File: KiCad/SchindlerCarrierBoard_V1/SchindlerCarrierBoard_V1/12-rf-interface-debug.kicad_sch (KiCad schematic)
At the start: 13 parts, among them J1200 u.FL -> A3, J1201 6-pin -> A3, J1202 JTAG, J1203 UART debug, J1204 2x20 expansion, SW1200 boot strap, SW1201 PS POR, SW1202 PL reset

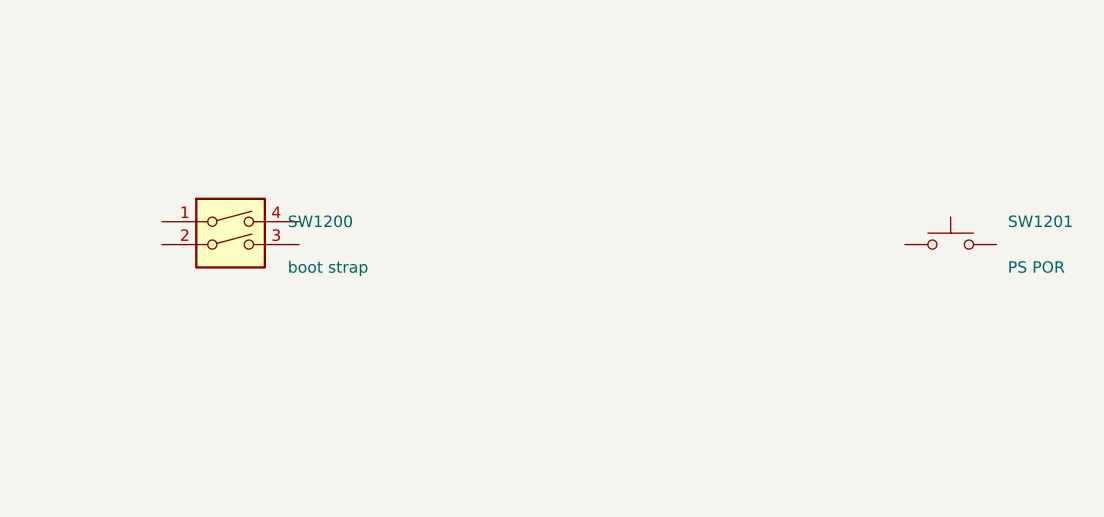
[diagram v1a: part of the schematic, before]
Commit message: Schindler carrier: ADV7511 R_EXT/AVDD fix + symbol relabel; 116 PL nets wired; connector/riser decisions
- U403 ADV7511: add R406 (887R 1%) pin28 R_EXT->GND; wire pin29 AVDD->+1V8_A (match 34/41).
  Sheet-4 ERC pin_not_connected 2->0. Fixes missing TMDS bias ref + unpowered AVDD
  (would-not-work HDMI-out bug, caught pre-fab).
- JustinLibrary ADV7511KSTZ symbol relabel: pin2 SYNC->VSYNC, 28 EXT->R_EXT, 29 R_EXT->AVDD
  (cosmetic; connectivity is by pin number). [NOTE: JustinLibrary is unversioned/external — not in this repo; see report.]
- Pin-lock: 116 PL nets wired; ERC unconnected 899->668; schindler_plio.xdc + pin-lock-assignment.md.
- Connector domain + analog I/O riser decided (connector-domain.md); riser-mezzanine-plan.md rev2
  (gated proposal, not implemented).
- bom-v1 (R406), refdes-map (R406 + symbol-mislabel note), changelog.

Deferred to next commit (kept out so this push stays honest): eeschema Update Symbols from
Library on U403 (display refresh); netlist regen; HDMI +5V power_pin_not_driven x2 (J400/J401.18)
verification; riser stays gated.

Co-Authored-By: Claude Opus 4.8 (1M context) <noreply@anthropic.com>
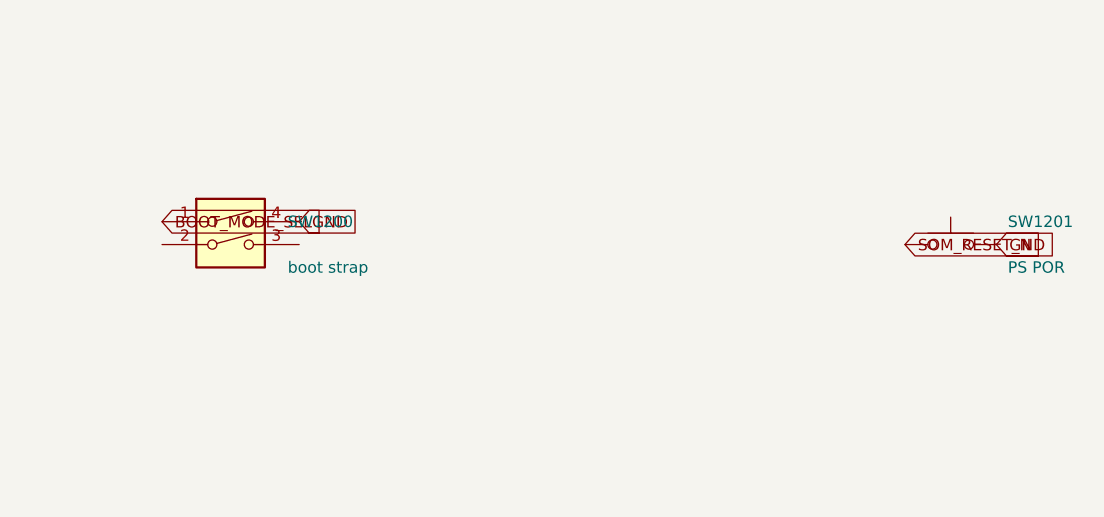
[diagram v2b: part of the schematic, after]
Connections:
- net GND: now also SW1200.4, SW1201.2
- net BOOT_MODE_SEL: now reaches SW1200.1
- net SOM_RESET_N: now reaches SW1201.1
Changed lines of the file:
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@@
+	(global_label "GND"
+		(shape input)
+		(at 438.15 27.94 0)
+		(effects
+			(font
+				(size 1.27 1.27)
+			)
+			(justify left)
+		)
+		(property "Intersheetrefs" "${INTERSHEET_REFS}"
+			(at 438.15 27.94 0)
+			(hide yes)
+			(show_name no)
+			(do_not_autoplace no)
+			(effects
+				(font
+					(size 1.27 1.27)
+				)
+			)
+		)
+	)
 	(global_label "GND"
 		(shape input)
@@
 			(hide yes)
 			(show_name no)
+			(do_not_autoplace no)
+			(effects
+				(font
+					(size 1.27 1.27)
+				)
+			)
+		)
+	)
+	(global_label "SOM_RESET_N"
+		(shape input)
+		(at 505.46 30.48 0)
+		(effects
+			(font
+				(size 1.27 1.27)
+			)
+			(justify left)
+		)
+		(property "Intersheetrefs" "${INTERSHEET_REFS}"
+			(at 505.46 30.48 0)
+			(hide yes)
+			(show_name no)
+			(do_not_autoplace no)
+			(effects
+				(font
+					(size 1.27 1.27)
+				)
+			)
+		)
+	)
+	(global_label "GND"
+		(shape input)
+		(at 515.62 30.48 0)
+		(effects
+			(font
+				(size 1.27 1.27)
+			)
+			(justify left)
+		)
+		(property "Intersheetrefs" "${INTERSHEET_REFS}"
+			(at 515.62 30.48 0)
+			(hide yes)
+			(show_name no)
+			(do_not_autoplace no)
+			(effects
+				(font
+					(size 1.27 1.27)
+				)
+			)
+		)
+	)
+	(global_label "BOOT_MODE_SEL"
+		(shape input)
+		(at 422.91 27.94 0)
+		(effects
+			(font
+				(size 1.27 1.27)
+			)
+			(justify left)
+		)
+		(property "Intersheetrefs" "${INTERSHEET_REFS}"
+			(at 422.91 27.94 0)
+			(hide yes)
+			(show_name no)
